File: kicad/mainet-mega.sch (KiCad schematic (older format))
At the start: 30 parts, among them J1 Screw_Terminal_01x03, J10 Screw_Terminal_01x03, J11 Screw_Terminal_01x03, J12 Screw_Terminal_01x03, J13 Screw_Terminal_01x03, J14 Screw_Terminal_01x03, J15 Screw_Terminal_01x03, J16 Screw_Terminal_01x03, J17 Screw_Terminal_01x03, J18 Screw_Terminal_01x03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

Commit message: KICAD: Agregar cambios esquemático del generador rotacional de pulsos
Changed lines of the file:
@@
 F0 "mainet-mega-rotary-pulse" 50
 F1 "mainet-mega-rotary-pulse.sch" 50
-F2 "rotaryPulseInput" I L 6100 4550 50
+F2 "rotaryPulseOutput" I L 6100 4550 50
 $EndSheet
 $Sheet

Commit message: KICAD: Guardar cambios sch del control de frecuencia M400
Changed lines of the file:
@@
 F0 "mainet-mega-rotary-pulse" 50
 F1 "mainet-mega-rotary-pulse.sch" 50
-F2 "rotaryPulseOutput" I L 6100 4550 50
+F2 "rotaryPulseOutput24V" I L 6100 4550 50
 $EndSheet
 $Sheet

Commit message: KICAD: Modificar sch del RPG
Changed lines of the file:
@@
 	5650 4550 6100 4550
-$Sheet
-S 6100 4300 1500 500
-U 5FC3A1C1
-F0 "mainet-mega-rotary-pulse" 50
-F1 "mainet-mega-rotary-pulse.sch" 50
-F2 "rotaryPulseOutput24V" I L 6100 4550 50
-$EndSheet
 $Sheet
 S 9100 4900 1500 500
@@
 F1 "mainet-mega-regleta-conexiones-motores.sch" 50
 $EndSheet
+$Sheet
+S 6100 4300 1500 500
+U 5FC3A1C1
+F0 "mainet-mega-rotary-pulse" 50
+F1 "mainet-mega-rotary-pulse.sch" 50
+F2 "rotaryPulseOutput5V" I L 6100 4550 50
+$EndSheet
 $EndSCHEMATC

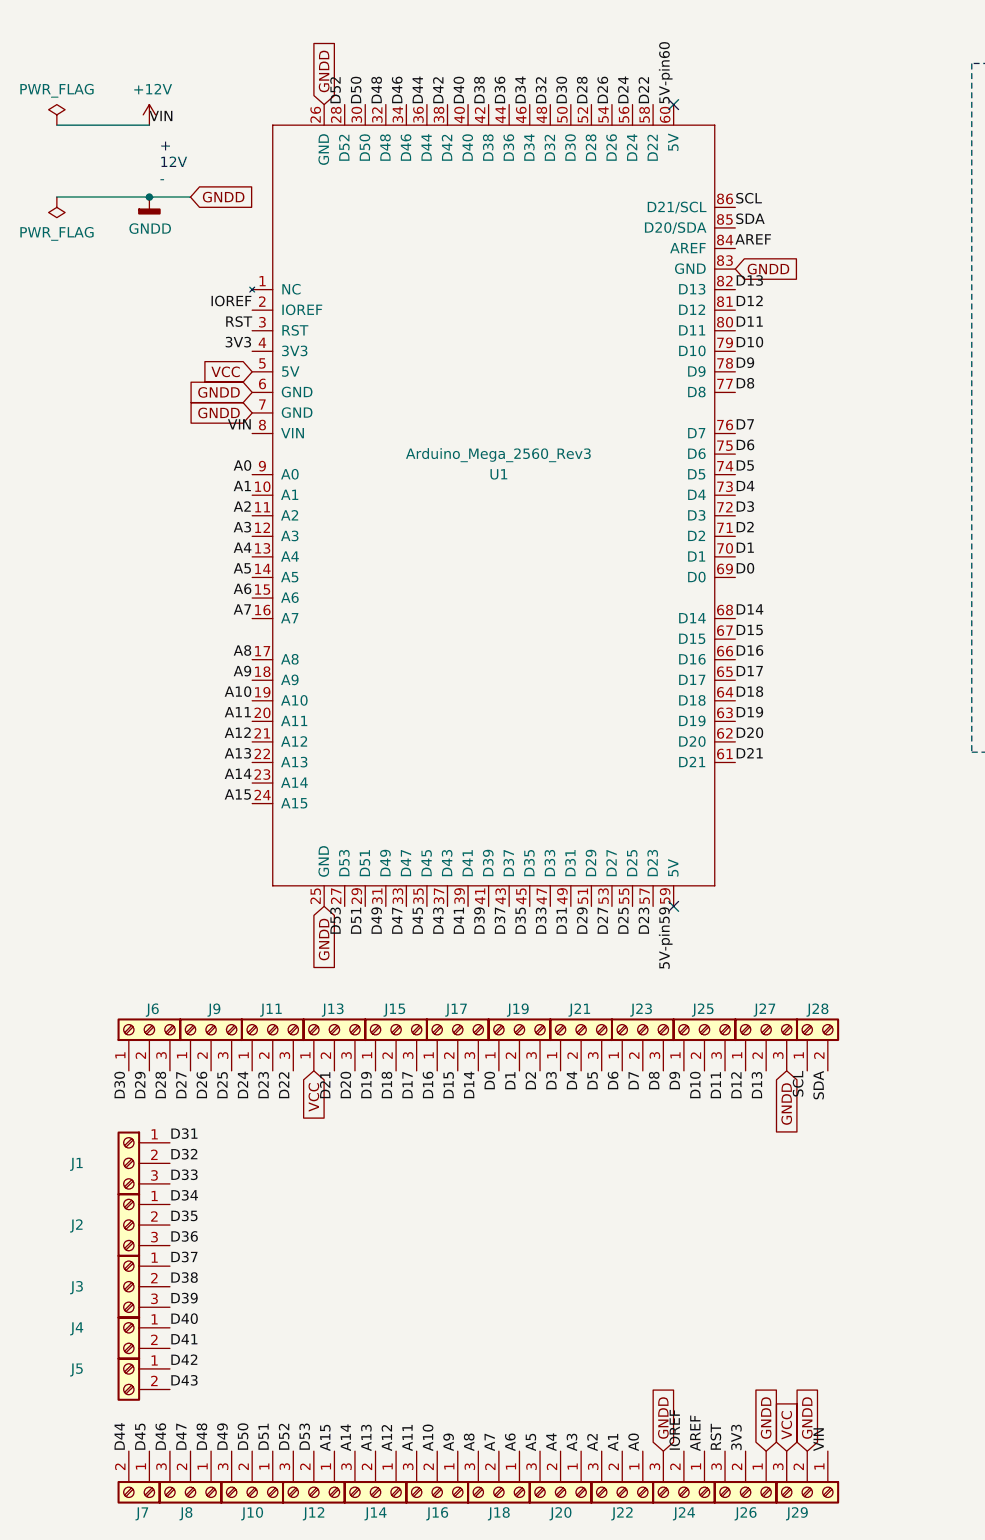
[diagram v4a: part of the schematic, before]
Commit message: KICAD: Incluir power jack en el .sch
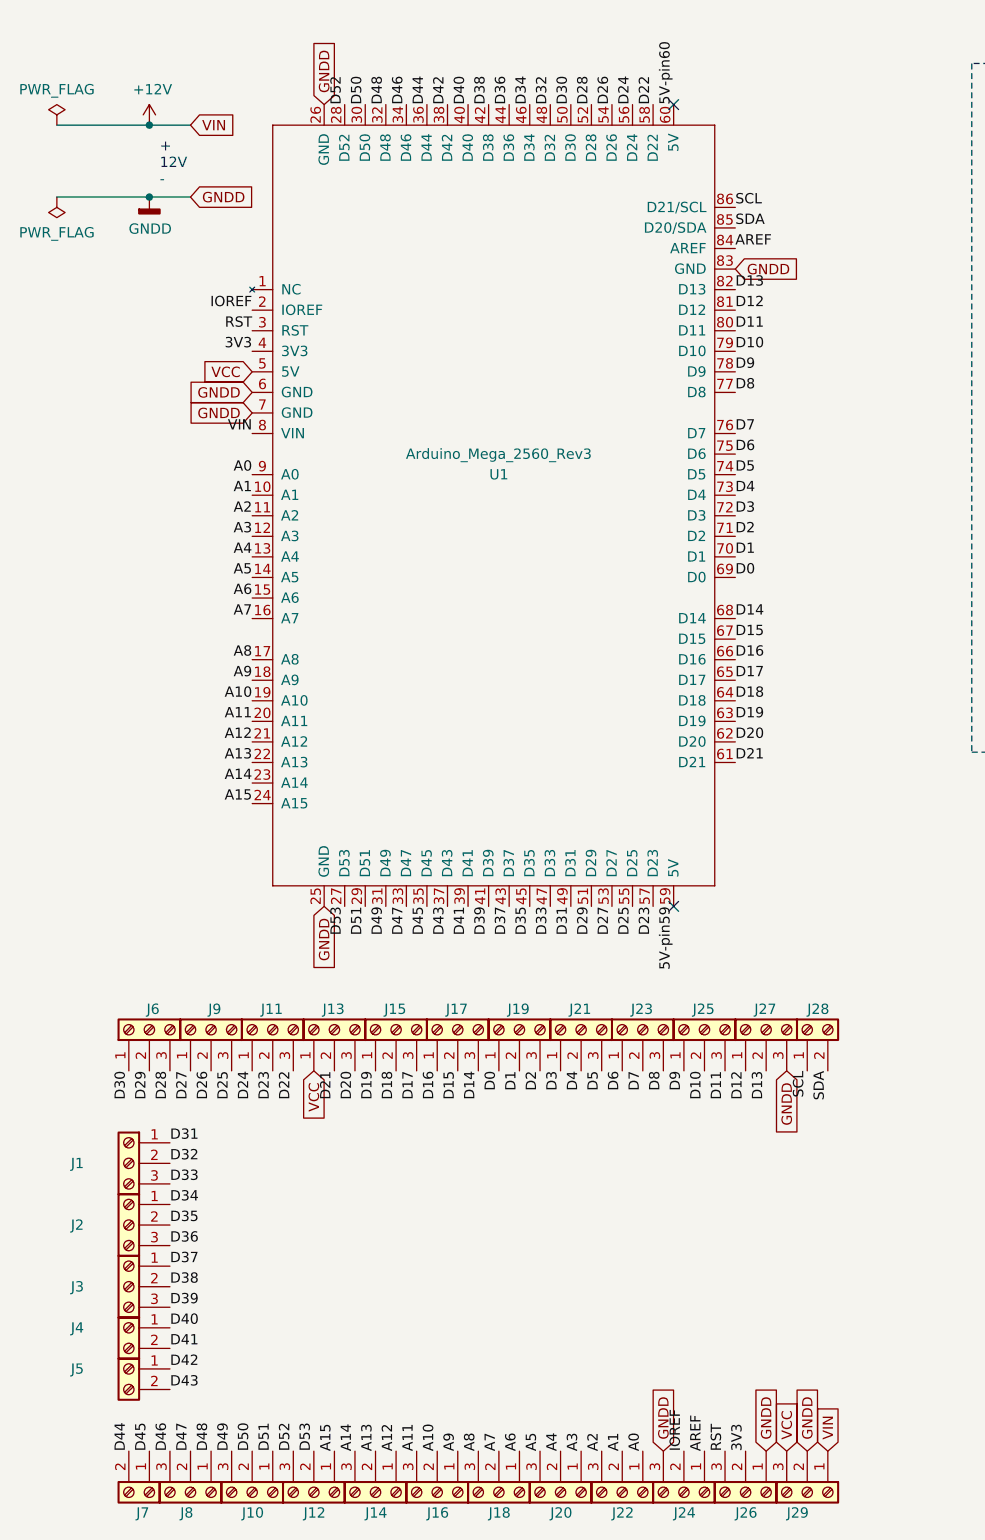
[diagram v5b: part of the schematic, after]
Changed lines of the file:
@@
 Text Label 4100 7350 1    50   ~ 0
 3V3
-Text Label 4500 7350 1    50   ~ 0
-VIN
 Text Label 1100 7350 1    50   ~ 0
 D44
@@
 	1    0    0    -1
 $EndComp
-Text Label 1200 900  0    50   ~ 0
-VIN
 Wire Wire Line
 	750  900  1200 900
@@
 F2 "rotaryPulseOutput5V" I L 6100 4550 50
 $EndSheet
+Text GLabel 4500 7350 1    50   Input ~ 0
+VIN
+Text GLabel 1400 900  2    50   Input ~ 0
+VIN
+Wire Wire Line
+	1400 900  1200 900
+Connection ~ 1200 900
 $EndSCHEMATC

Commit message: KICAD: Actualizar archivos sch
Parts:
- added C1: 47uF, symbol Device:C
- added C2: 100nF, symbol Device:C
- added D26: D, symbol Device:D
- added J101: PWRIN, symbol Connector:Barrel_Jack_Switch
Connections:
- net +12V: now also D26.2 (A), J101.1; no longer J29.1 (Pin_1), U1.8 (VIN)
- net GNDD: now also C1.2, C2.2, J101.2, J101.3
- new net VIN: C1.1, C2.1, D26.1 (K), J29.1 (Pin_1), U1.8 (VIN)
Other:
- note removed: "+\n12V\n-\n"
- moved on the sheet: J1, J10, J11, J12, J13, J14, J15, J16, J17, J18, J19, J2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

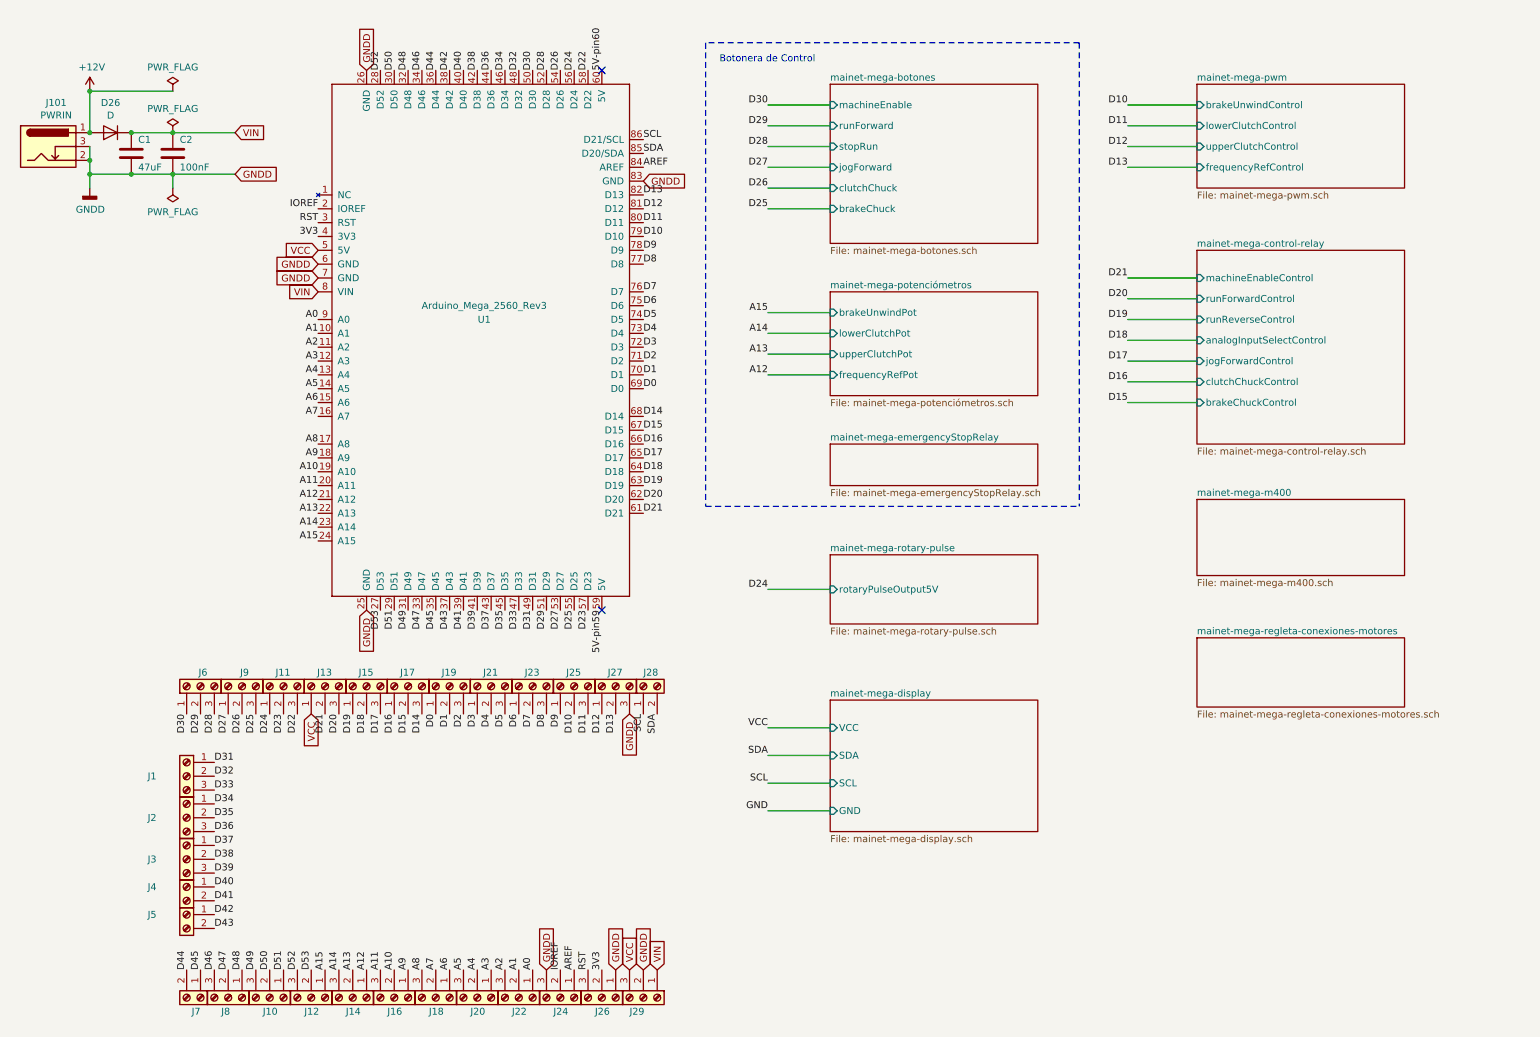
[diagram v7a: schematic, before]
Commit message: KICAD: Corregir pines de salida digital del Arduino para control de relés y pines de cableado con la pantalla Nextion
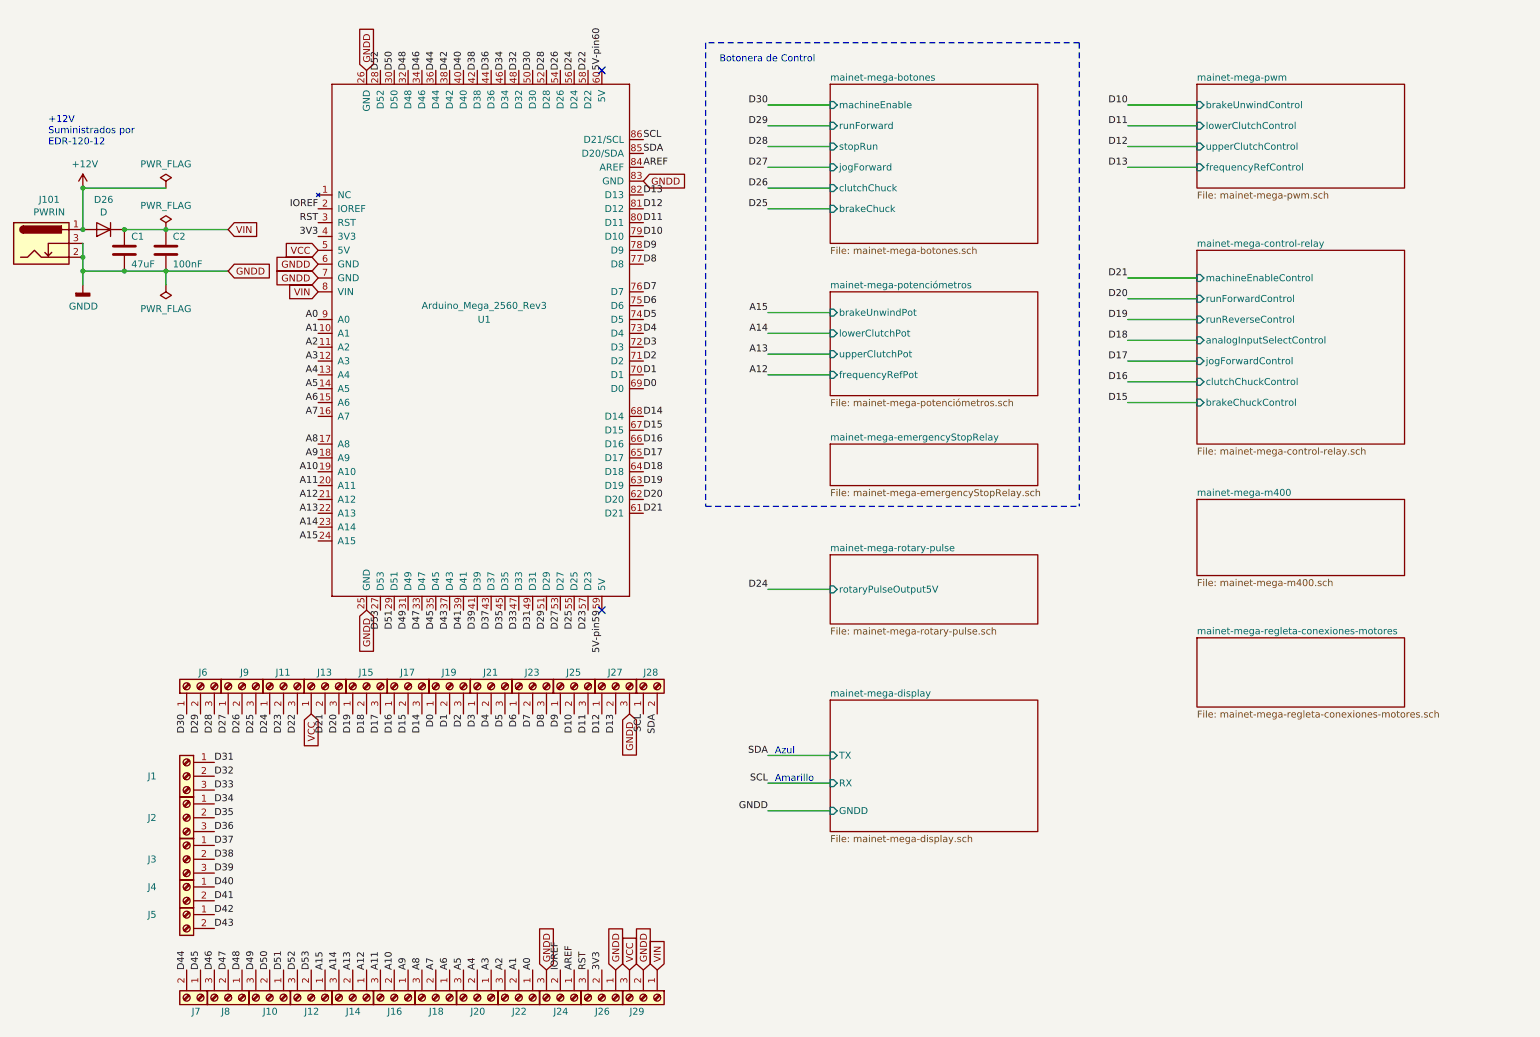
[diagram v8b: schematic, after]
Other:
- note added: "+12V\nSuministrados por\nEDR-120-12"
- note added: "Amarillo"
- note added: "Azul"
- moved on the sheet: C1, C2, D26, J101
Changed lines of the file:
@@
 L power:PWR_FLAG #FLG02
 U 1 1 5FD8CEEC
-P 1700 1650
-F 0 "#FLG02" H 1700 1725 50  0001 C CNN
-F 1 "PWR_FLAG" H 1700 1823 50  0000 C CNN
-F 2 "" H 1700 1650 50  0001 C CNN
-F 3 "~" H 1700 1650 50  0001 C CNN
-	1    1700 1650
+P 1650 2350
+F 0 "#FLG02" H 1650 2425 50  0001 C CNN
+F 1 "PWR_FLAG" H 1650 2523 50  0000 C CNN
+F 2 "" H 1650 2350 50  0001 C CNN
+F 3 "~" H 1650 2350 50  0001 C CNN
+	1    1650 2350
 	1    0    0    1
 $EndComp
@@
 F0 "mainet-mega-display" 50
 F1 "mainet-mega-display.sch" 50
-F2 "VCC" I L 6450 5550 50
-F3 "SDA" I L 6450 5750 50
-F4 "SCL" I L 6450 5950 50
-F5 "GND" I L 6450 6150 50
+F2 "TX" I L 6450 5750 50
+F3 "RX" I L 6450 5950 50
+F4 "GNDD" I L 6450 6150 50
 $EndSheet
-Text Label 6000 5550 2    50   ~ 0
-VCC
 Text Label 6000 5750 2    50   ~ 0
 SDA
@@
 SCL
 Text Label 6000 6150 2    50   ~ 0
-GND
-Wire Wire Line
-	6000 5550 6450 5550
+GNDD
 Wire Wire Line
 	6000 5750 6450 5750
@@
 L power:+12V #PWR01
 U 1 1 5FDD8047
-P 1100 950
-F 0 "#PWR01" H 1100 800 50  0001 C CNN
-F 1 "+12V" H 1115 1123 50  0000 C CNN
-F 2 "" H 1100 950 50  0001 C CNN
-F 3 "" H 1100 950 50  0001 C CNN
-	1    1100 950
+P 1050 1650
+F 0 "#PWR01" H 1050 1500 50  0001 C CNN
+F 1 "+12V" H 1065 1823 50  0000 C CNN
+F 2 "" H 1050 1650 50  0001 C CNN
+F 3 "" H 1050 1650 50  0001 C CNN
+	1    1050 1650
 	1    0    0    -1
 $EndComp
@@
 Text GLabel 2700 5450 3    50   Input ~ 0
 VCC
-Text GLabel 2150 1550 2    50   Input ~ 0
+Text GLabel 2100 2250 2    50   Input ~ 0
 GNDD
 $Sheet
@@
 Text GLabel 5200 7300 1    50   Input ~ 0
 VIN
-Text GLabel 2150 1250 2    50   Input ~ 0
+Text GLabel 2100 1950 2    50   Input ~ 0
 VIN
 $Comp
 L Connector:Barrel_Jack_Switch J101
 U 1 1 60E2C078
-P 800 1350
-F 0 "J101" H 857 1667 50  0000 C CNN
-F 1 "PWRIN" H 857 1576 50  0000 C CNN
-F 2 "" H 850 1310 50  0001 C CNN
-F 3 "~" H 850 1310 50  0001 C CNN
-	1    800  1350
+P 750 2050
+F 0 "J101" H 807 2367 50  0000 C CNN
+F 1 "PWRIN" H 807 2276 50  0000 C CNN
+F 2 "" H 800 2010 50  0001 C CNN
+F 3 "~" H 800 2010 50  0001 C CNN
+	1    750  2050
 	1    0    0    -1
 $EndComp
@@
 L Device:D D26
 U 1 1 60E39489
-P 1250 1250
-F 0 "D26" H 1250 1034 50  0000 C CNN
-F 1 "D" H 1250 1125 50  0000 C CNN
-F 2 "" H 1250 1250 50  0001 C CNN
-F 3 "~" H 1250 1250 50  0001 C CNN
-	1    1250 1250
+P 1200 1950
+F 0 "D26" H 1200 1734 50  0000 C CNN
+F 1 "D" H 1200 1825 50  0000 C CNN
+F 2 "" H 1200 1950 50  0001 C CNN
+F 3 "~" H 1200 1950 50  0001 C CNN
+	1    1200 1950
 	-1   0    0    1
 $EndComp
@@
 L Device:C C1
 U 1 1 60E3D7F0
-P 1400 1400
-F 0 "C1" H 1450 1500 50  0000 L CNN
-F 1 "47uF" H 1450 1300 50  0000 L CNN
-F 2 "" H 1438 1250 50  0001 C CNN
-F 3 "~" H 1400 1400 50  0001 C CNN
-	1    1400 1400
+P 1350 2100
+F 0 "C1" H 1400 2200 50  0000 L CNN
+F 1 "47uF" H 1400 2000 50  0000 L CNN
+F 2 "" H 1388 1950 50  0001 C CNN
+F 3 "~" H 1350 2100 50  0001 C CNN
+	1    1350 2100
 	1    0    0    -1
 $EndComp
@@
 L Device:C C2
 U 1 1 60E3E6FC
-P 1700 1400
-F 0 "C2" H 1750 1500 50  0000 L CNN
-F 1 "100nF" H 1750 1300 50  0000 L CNN
-F 2 "" H 1738 1250 50  0001 C CNN
-F 3 "~" H 1700 1400 50  0001 C CNN
-	1    1700 1400
+P 1650 2100
+F 0 "C2" H 1700 2200 50  0000 L CNN
+F 1 "100nF" H 1700 2000 50  0000 L CNN
+F 2 "" H 1688 1950 50  0001 C CNN
+F 3 "~" H 1650 2100 50  0001 C CNN
+	1    1650 2100
 	1    0    0    -1
 $EndComp
 Wire Wire Line
-	1400 1250 1700 1250
-Connection ~ 1400 1250
-Wire Wire Line
-	1100 950  1100 1250
-Connection ~ 1100 1250
-Connection ~ 1100 950
+	1350 1950 1650 1950
+Connection ~ 1350 1950
+Wire Wire Line
+	1050 1650 1050 1950
+Connection ~ 1050 1950
+Connection ~ 1050 1650
 $Comp
 L power:GNDD #PWR02
 U 1 1 60E45FE4
-P 1100 1650
-F 0 "#PWR02" H 1100 1400 50  0001 C CNN
-F 1 "GNDD" H 1104 1495 50  0000 C CNN
-F 2 "" H 1100 1650 50  0001 C CNN
-F 3 "" H 1100 1650 50  0001 C CNN
-	1    1100 1650
+P 1050 2350
+F 0 "#PWR02" H 1050 2100 50  0001 C CNN
+F 1 "GNDD" H 1054 2195 50  0000 C CNN
+F 2 "" H 1050 2350 50  0001 C CNN
+F 3 "" H 1050 2350 50  0001 C CNN
+	1    1050 2350
 	1    0    0    -1
 $EndComp
 Wire Wire Line
-	1100 1550 1400 1550
-Connection ~ 1400 1550
-Wire Wire Line
-	1400 1550 1700 1550
-Connection ~ 1700 1550
-Connection ~ 1700 1250
-Wire Wire Line
-	1700 1250 2150 1250
-Wire Wire Line
-	1700 1550 2150 1550
-Wire Wire Line
-	1100 1350 1100 1450
-Wire Wire Line
-	1100 1450 1100 1550
-Connection ~ 1100 1450
-Connection ~ 1100 1550
-Wire Wire Line
-	1100 1550 1100 1650
-Wire Wire Line
-	1100 950  1700 950
-Wire Wire Line
-	1700 1650 1700 1550
+	1050 2250 1350 2250
+Connection ~ 1350 2250
+Wire Wire Line
+	1350 2250 1650 2250
+Connection ~ 1650 2250
+Connection ~ 1650 1950
+Wire Wire Line
+	1650 1950 2100 1950
+Wire Wire Line
+	1650 2250 2100 2250
+Wire Wire Line
+	1050 2050 1050 2150
+Wire Wire Line
+	1050 2150 1050 2250
+Connection ~ 1050 2150
+Connection ~ 1050 2250
+Wire Wire Line
+	1050 2250 1050 2350
+Wire Wire Line
+	1050 1650 1650 1650
+Wire Wire Line
+	1650 2350 1650 2250
 Text GLabel 2750 2400 0    50   Input ~ 0
 VIN
@@
 L power:PWR_FLAG #FLG0101
 U 1 1 60E6AE09
-P 1700 1250
-F 0 "#FLG0101" H 1700 1325 50  0001 C CNN
-F 1 "PWR_FLAG" H 1700 1423 50  0000 C CNN
-F 2 "" H 1700 1250 50  0001 C CNN
-F 3 "~" H 1700 1250 50  0001 C CNN
-	1    1700 1250
+P 1650 1950
+F 0 "#FLG0101" H 1650 2025 50  0001 C CNN
+F 1 "PWR_FLAG" H 1650 2123 50  0000 C CNN
+F 2 "" H 1650 1950 50  0001 C CNN
+F 3 "~" H 1650 1950 50  0001 C CNN
+	1    1650 1950
 	1    0    0    -1
 $EndComp
@@
 L power:PWR_FLAG #FLG01
 U 1 1 5FB921DC
-P 1700 950
-F 0 "#FLG01" H 1700 1025 50  0001 C CNN
-F 1 "PWR_FLAG" H 1700 1123 50  0000 C CNN
-F 2 "" H 1700 950 50  0001 C CNN
-F 3 "~" H 1700 950 50  0001 C CNN
-	1    1700 950
+P 1650 1650
+F 0 "#FLG01" H 1650 1725 50  0001 C CNN
+F 1 "PWR_FLAG" H 1650 1823 50  0000 C CNN
+F 2 "" H 1650 1650 50  0001 C CNN
+F 3 "~" H 1650 1650 50  0001 C CNN
+	1    1650 1650
 	1    0    0    -1
 $EndComp
+Text Notes 6050 5750 0    50   ~ 0
+Azul
+Text Notes 6050 5950 0    50   ~ 0
+Amarillo
+Text Notes 800  1350 0    50   ~ 0
++12V\nSuministrados por\nEDR-120-12
 $EndSCHEMATC
